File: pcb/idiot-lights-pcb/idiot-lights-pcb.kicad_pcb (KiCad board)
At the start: 2 copper layers, 100.3 x 66 mm, 35 parts, among them SW1 Toggle left indicator, SW2 Toggle right indicator, SW3 Toggle hazard warning, SW4 Break control, SW5 Reset

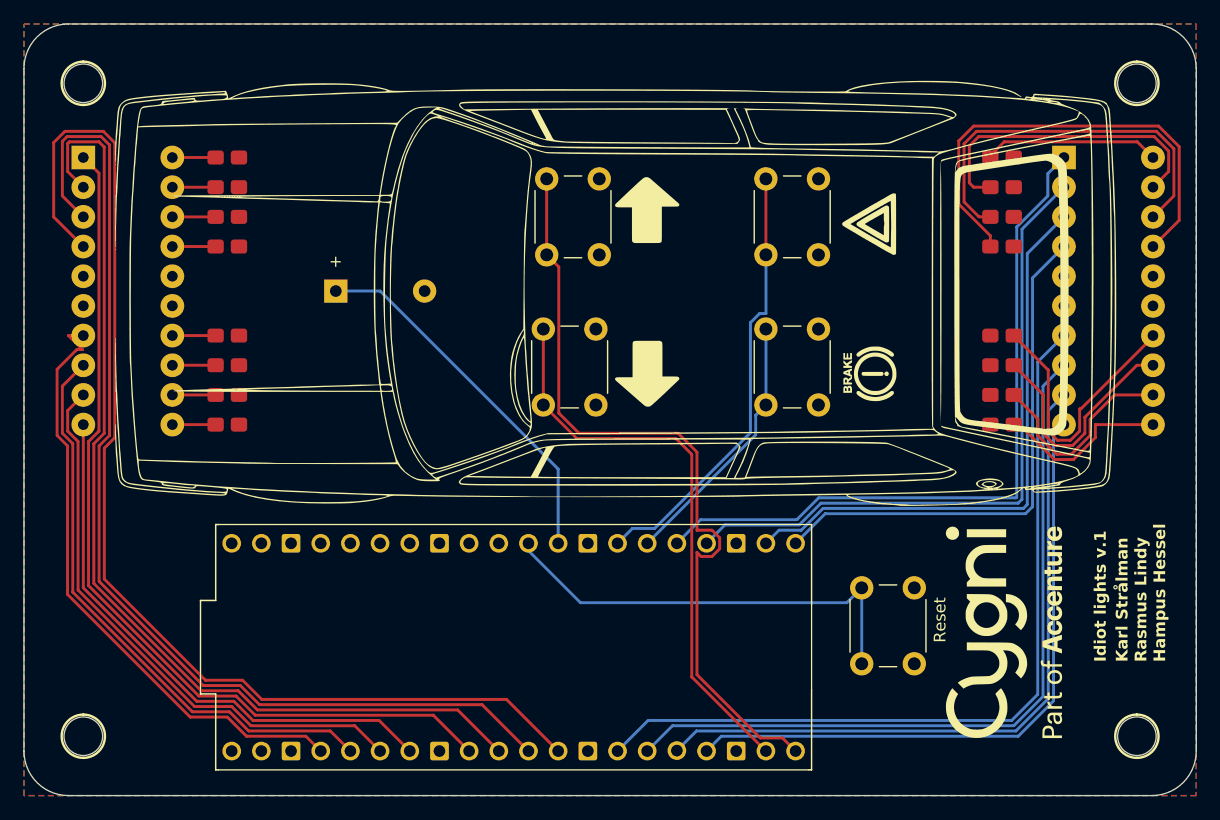
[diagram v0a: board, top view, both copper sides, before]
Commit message: Switch from THT to SMD for multiple components
Buzzer & LED lights arrays
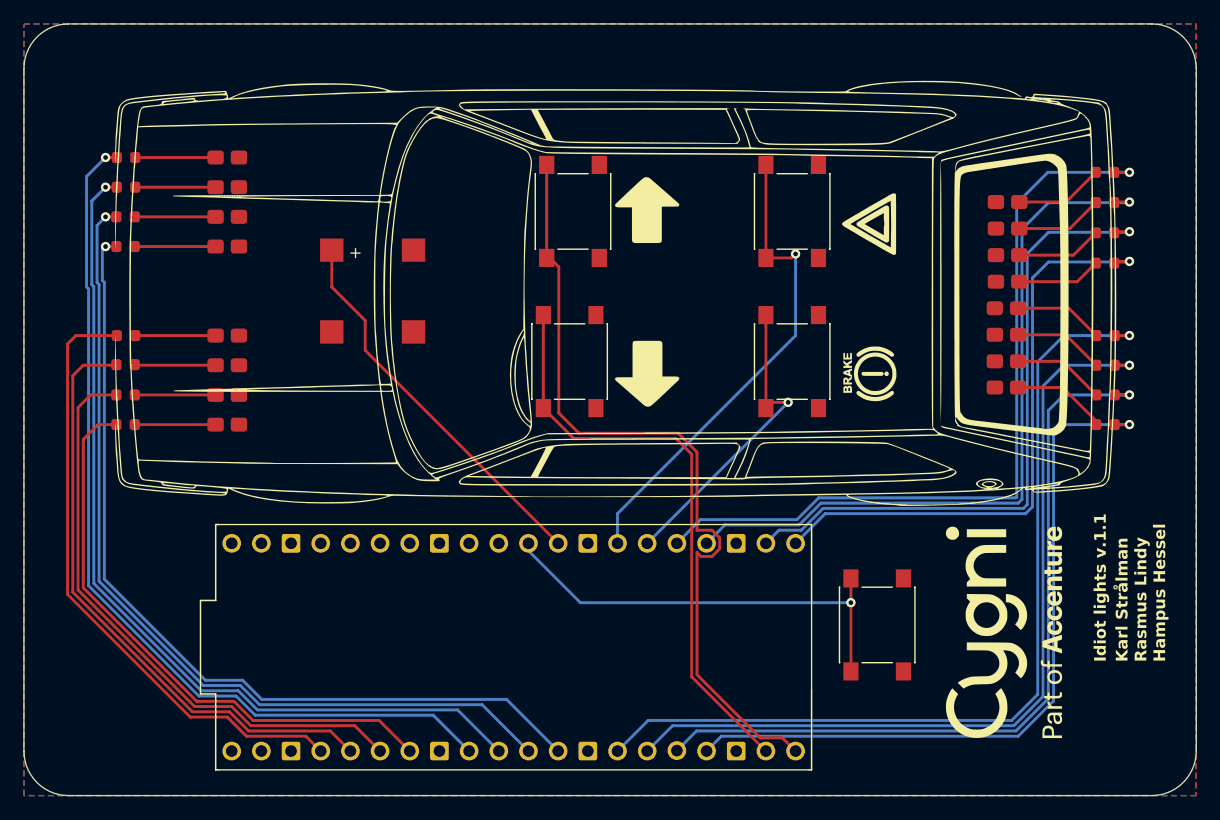
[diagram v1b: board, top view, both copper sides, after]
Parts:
- removed >NAME (x4): >VALUE, Hardware:STAND-OFF
- removed BAR1, BAR2: HDSP-4830_2, Display:HDSP-4830
- added D1: LED, LED_SMD_no_silk:LED_0603_1608Metric_no_silk, F.Cu at (143.3, 71.1)
- added D10: LED, LED_SMD_no_silk:LED_0603_1608Metric_no_silk, F.Cu at (227.2, 68.6)
- added D11: LED, LED_SMD_no_silk:LED_0603_1608Metric_no_silk, F.Cu at (227.2, 66.0)
- added D12: LED, LED_SMD_no_silk:LED_0603_1608Metric_no_silk, F.Cu at (227.2, 63.5)
- added D13: LED, LED_SMD_no_silk:LED_0603_1608Metric_no_silk, F.Cu at (227.1, 57.3)
- added D14: LED, LED_SMD_no_silk:LED_0603_1608Metric_no_silk, F.Cu at (227.1, 54.7)
- added D15: LED, LED_SMD_no_silk:LED_0603_1608Metric_no_silk, F.Cu at (227.1, 52.1)
- added D16: LED, LED_SMD_no_silk:LED_0603_1608Metric_no_silk, F.Cu at (227.1, 49.5)
- added D2: LED, LED_SMD_no_silk:LED_0603_1608Metric_no_silk, F.Cu at (143.3, 68.6)
- added D3: LED, LED_SMD_no_silk:LED_0603_1608Metric_no_silk, F.Cu at (143.3, 66.0)
- added D4: LED, LED_SMD_no_silk:LED_0603_1608Metric_no_silk, F.Cu at (143.4, 63.5)
- added D5: LED, LED_SMD_no_silk:LED_0603_1608Metric_no_silk, F.Cu at (143.3, 55.9)
- added D6: LED, LED_SMD_no_silk:LED_0603_1608Metric_no_silk, F.Cu at (143.3, 53.3)
- added D7: LED, LED_SMD_no_silk:LED_0603_1608Metric_no_silk, F.Cu at (143.4, 50.8)
- added D8: LED, LED_SMD_no_silk:LED_0603_1608Metric_no_silk, F.Cu at (143.4, 48.3)
- added D9: LED, LED_SMD_no_silk:LED_0603_1608Metric_no_silk, F.Cu at (227.2, 71.1)
- BZ1: footprint Buzzer_Beeper:Buzzer_12x9.5RM7.6 -> Buzzer_Beeper:PUIAudio_SMT_0825_S_4_R
- SW1, SW2, SW3, SW4, SW5: footprint Button_Switch_THT:SW_PUSH_6mm_H5mm -> Button_Switch_SMD:SW_SPST_PTS645
- moved SW1 4.34 mm to (181.3, 65.7)
- moved SW2 4.34 mm to (181.6, 52.9)
- moved SW3 4.34 mm to (200.4, 52.9)
- moved SW4 4.34 mm to (200.4, 65.7)
- moved R16 3.84 mm to (218.8, 52.1), turned to 180 degrees
- moved SW5 3.58 mm to (207.6, 88.3)
- moved R15 3.57 mm to (218.8, 54.3), turned to 180 degrees
- moved R14 3.31 mm to (218.8, 56.6), turned to 180 degrees
- moved R9 3.20 mm to (218.7, 67.9)
- moved BZ1 3.16 mm to (164.5, 59.7)
- moved R13 3.04 mm to (218.8, 58.9), turned to 180 degrees
- moved R10 2.90 mm to (218.7, 65.7)
- moved R11 2.64 mm to (218.7, 63.4)
- moved R12 2.37 mm to (218.7, 61.2)
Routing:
- net Net-(D13-K): track 39.8 -> 7.20 mm
- net Net-(D14-K): track 33.3 -> 7.33 mm
- net /FR3: track 98.6 -> 74.5 mm, vias 0 -> 1
- net Net-(D15-K): track 26.7 -> 7.47 mm
- net /FR2: track 92.2 -> 75.3 mm, vias 0 -> 1
- net Net-(D12-K): track 23.5 -> 7.65 mm
- net Net-(D11-K): track 20.4 -> 7.76 mm
- net /FR1: track 86.0 -> 76.0 mm, vias 0 -> 1
- net Net-(D10-K): track 17.8 -> 7.87 mm
- net Net-(D16-K): track 15.1 -> 7.60 mm
- net /RL3: track 55.5 -> 62.4 mm, vias 0 -> 1
- net /RL2: track 60.2 -> 67.1 mm, vias 0 -> 1
- net /RL0: track 69.6 -> 76.5 mm, vias 0 -> 1
- net /RL1: track 64.9 -> 71.8 mm, vias 0 -> 1
- net Net-(D9-K): track 15.0 -> 8.17 mm
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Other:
- board text added: "Idiot lights v.1.1"
- board text removed: "Idiot lights v.1"

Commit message: Add pico SMD solder mounts
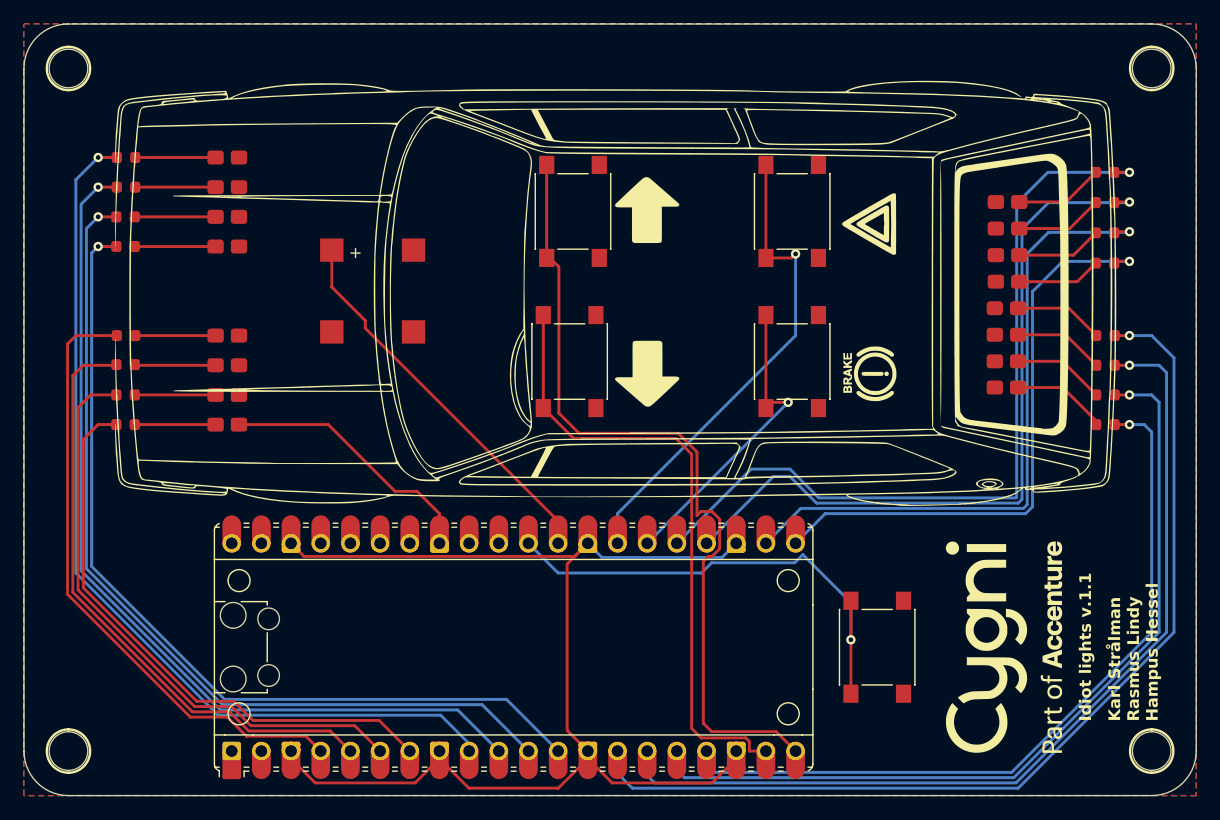
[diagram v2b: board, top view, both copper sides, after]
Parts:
- removed A1: SC0915, Raspberry_Pi_Pico_Kicad_Files:MODULE_SC0915
- added >NAME: >VALUE, Hardware:STAND-OFF, F.Cu at (138.4, 99.1)
- added >NAME: >VALUE, Hardware:STAND-OFF, F.Cu at (231.1, 99.1)
- added >NAME: >VALUE, Hardware:STAND-OFF, F.Cu at (231.1, 40.6)
- added >NAME: >VALUE, Hardware:STAND-OFF, F.Cu at (138.4, 40.6)
- added U1: RaspberryPi_Pico, Module_RaspberryPi_Pico:RaspberryPi_Pico_Common, F.Cu at (176.5, 90.2)
- moved SW5 1.91 mm to (207.6, 90.2)
- moved G*** 1.27 mm to (218.4, 90.2)
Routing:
- net Net-(U1-GND-Pad13): track 0.00 -> 105.5 mm
- net GND: track 0.00 -> 22.9 mm
- net /RL0: track 76.5 -> 84.9 mm
- net /RL1: track 71.8 -> 79.1 mm
- net /RL2: track 67.1 -> 72.1 mm
- net /RUN: track 37.8 -> 42.1 mm
- net /L_INDCR_BTN: track 50.1 -> 53.1 mm
- net /RL3: track 62.4 -> 65.1 mm
- net /RR0: track 67.9 -> 70.0 mm
- net /RR1: track 63.2 -> 65.1 mm
- net /FR0: track 76.8 -> 78.3 mm
- net /FR3: track 74.5 -> 75.6 mm
- net /FR1: track 76.0 -> 77.2 mm
- net /FR2: track 75.3 -> 76.4 mm
- net /R_INDCR_BTN: track 69.0 -> 70.1 mm
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
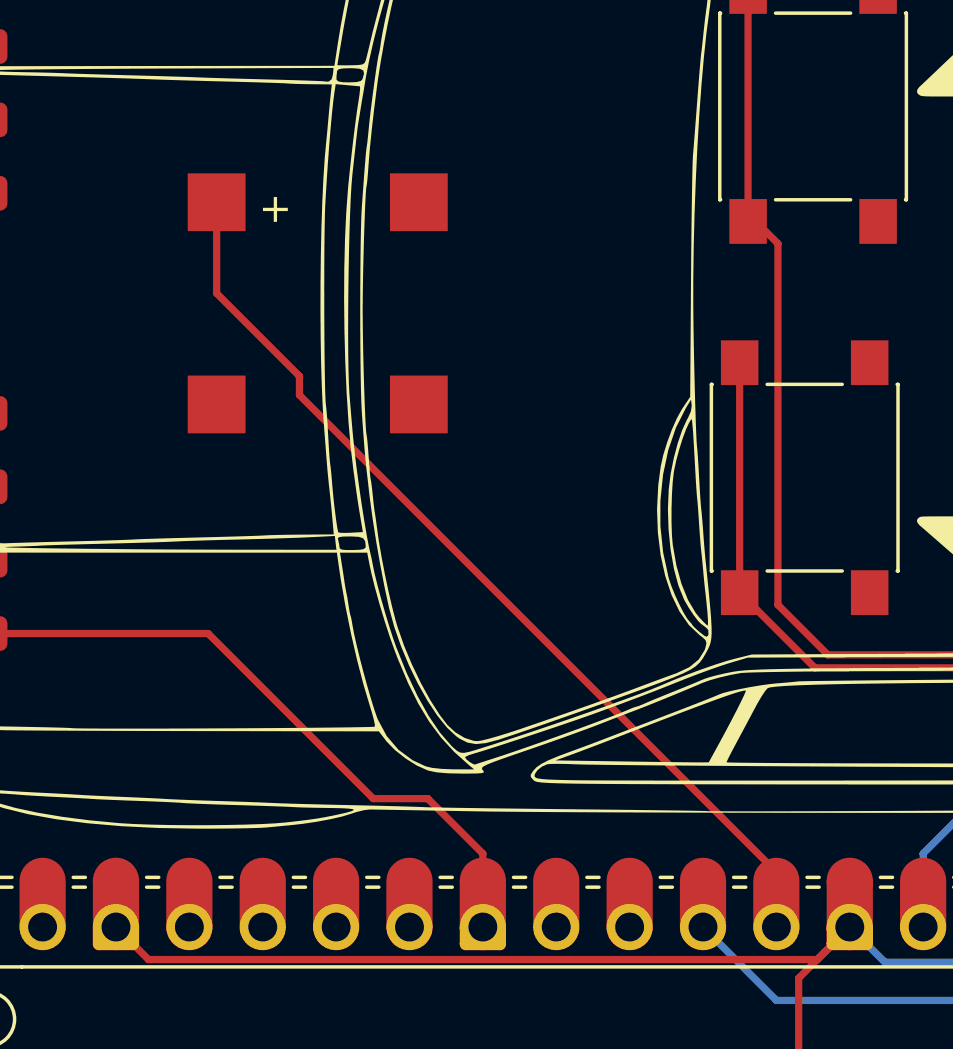
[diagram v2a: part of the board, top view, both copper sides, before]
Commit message: Replace buzzer with CPT
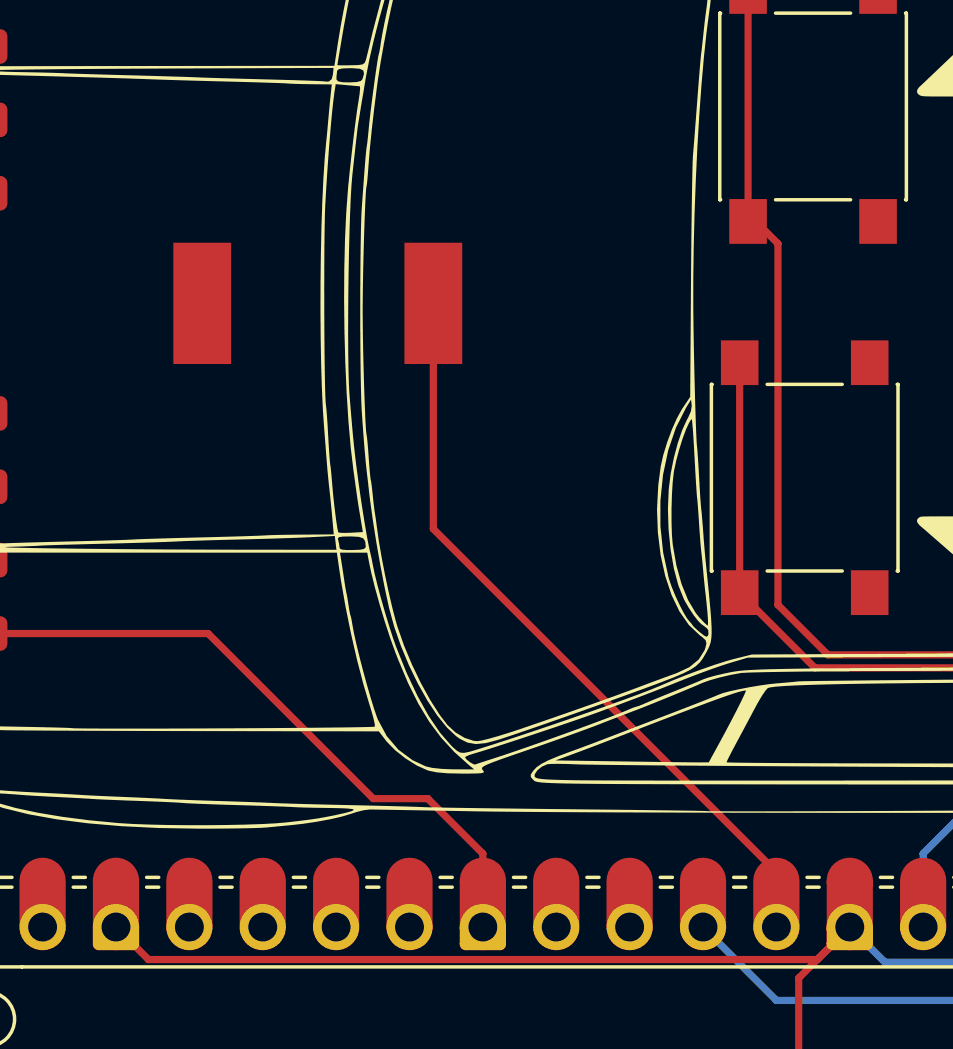
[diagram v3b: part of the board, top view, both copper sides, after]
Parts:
- BZ1: footprint Buzzer_Beeper:PUIAudio_SMT_0825_S_4_R -> Buzzer_Beeper:Buzzer_CUI_CPT-9019S-SMT
- turned BZ1 to 180 degrees
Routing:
- net /BUZZER: track 33.1 -> 26.5 mm
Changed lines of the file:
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@@
     )
   )
-  (footprint "Buzzer_Beeper:PUIAudio_SMT_0825_S_4_R" (layer "F.Cu")
-    (at 164.465 59.69)
-    (descr "SMD 8540, http://www.puiaudio.com/product-detail.aspx?partnumber=SMT-0825-S-4-R")
-    (tags "SMD 8540")
+  (footprint "Buzzer_Beeper:Buzzer_CUI_CPT-9019S-SMT" (layer "F.Cu")
+    (at 164.465 59.69 180)
+    (descr "https://www.cui.com/product/resource/cpt-9019s-smt.pdf")
+    (tags "buzzer piezo")
     (property "Sheetfile" "idiot-lights-pcb.kicad_sch")
     (property "Sheetname" "")
@@
     (property "ki_keywords" "quartz resonator ceramic")
     (attr smd)
-    (fp_text reference "BZ1" (at 0.2 -5.9) (layer "F.SilkS") hide
+    (fp_text reference "BZ1" (at 0 -5.5) (layer "F.SilkS") hide
         (effects (font (size 1 1) (thickness 0.15)))
     )
-    (fp_text value "Buzzer" (at 0.1 6) (layer "F.Fab") hide
-        (effects (font (size 1 1) (thickness 0.15)))
-    )
-    (fp_text user "+" (at -1.5 -3.25 270) (layer "F.SilkS")
-        (effects (font (size 1 1) (thickness 0.15)))
-    )
-    (fp_text user "+" (at -2.75 -2.75 270) (layer "F.Fab")
+    (fp_text value "Buzzer" (at 0 5.5) (layer "F.Fab") hide
         (effects (font (size 1 1) (thickness 0.15)))
     )
+    (fp_line (start -5.25 -2.35) (end -4.75 -2.35)
+      (stroke (width 0.05) (type solid)) (layer "F.CrtYd"))
+    (fp_line (start -5.25 2.35) (end -5.25 -2.35)
+      (stroke (width 0.05) (type solid)) (layer "F.CrtYd"))
     (fp_line (start -4.75 -4.75) (end 4.75 -4.75)
       (stroke (width 0.05) (type solid)) (layer "F.CrtYd"))
-    (fp_line (start -4.75 4.75) (end -4.75 -4.75)
+    (fp_line (start -4.75 -2.35) (end -4.75 -4.75)
+      (stroke (width 0.05) (type solid)) (layer "F.CrtYd"))
+    (fp_line (start -4.75 2.35) (end -5.25 2.35)
+      (stroke (width 0.05) (type solid)) (layer "F.CrtYd"))
+    (fp_line (start -4.75 4.75) (end -4.75 2.35)
       (stroke (width 0.05) (type solid)) (layer "F.CrtYd"))
-    (fp_line (start 4.75 -4.75) (end 4.75 4.75)
+    (fp_line (start 4.75 -4.75) (end 4.75 -2.35)
+      (stroke (width 0.05) (type solid)) (layer "F.CrtYd"))
+    (fp_line (start 4.75 -2.35) (end 5.25 -2.35)
+      (stroke (width 0.05) (type solid)) (layer "F.CrtYd"))
+    (fp_line (start 4.75 2.35) (end 4.75 4.75)
       (stroke (width 0.05) (type solid)) (layer "F.CrtYd"))
     (fp_line (start 4.75 4.75) (end -4.75 4.75)
       (stroke (width 0.05) (type solid)) (layer "F.CrtYd"))
-    (fp_line (start -4.25 -2.75) (end -2.75 -4.25)
-      (stroke (width 0.1) (type solid)) (layer "F.Fab"))
-    (fp_line (start -4.25 2.75) (end -4.25 -2.75)
-      (stroke (width 0.1) (type solid)) (layer "F.Fab"))
-    (fp_line (start -2.75 -4.25) (end 2.75 -4.25)
-      (stroke (width 0.1) (type solid)) (layer "F.Fab"))
-    (fp_line (start -2.75 4.25) (end -4.25 2.75)
+    (fp_line (start 5.25 -2.35) (end 5.25 2.35)
+      (stroke (width 0.05) (type solid)) (layer "F.CrtYd"))
+    (fp_line (start 5.25 2.35) (end 4.75 2.35)
+      (stroke (width 0.05) (type solid)) (layer "F.CrtYd"))
+    (fp_line (start -4.5 -3.5) (end -4.5 4.5)
       (stroke (width 0.1) (type solid)) (layer "F.Fab"))
-    (fp_line (start 2.75 -4.25) (end 4.25 -2.75)
+    (fp_line (start -4.5 4.5) (end 4.5 4.5)
       (stroke (width 0.1) (type solid)) (layer "F.Fab"))
-    (fp_line (start 2.75 4.25) (end -2.75 4.25)
+    (fp_line (start -3.5 -4.5) (end -4.5 -3.5)
       (stroke (width 0.1) (type solid)) (layer "F.Fab"))
-    (fp_line (start 4.25 -2.75) (end 4.25 2.75)
+    (fp_line (start 4.5 -4.5) (end -3.5 -4.5)
       (stroke (width 0.1) (type solid)) (layer "F.Fab"))
-    (fp_line (start 4.25 2.75) (end 2.75 4.25)
+    (fp_line (start 4.5 4.5) (end 4.5 -4.5)
       (stroke (width 0.1) (type solid)) (layer "F.Fab"))
-    (pad "1" smd rect (at -3.5 -3.5 270) (size 2 2) (layers "F.Cu" "F.Paste" "F.Mask")
+    (pad "1" smd rect (at -4 0 180) (size 2 4.2) (layers "F.Cu" "F.Paste" "F.Mask")
       (net 4 "/BUZZER") (pinfunction "-") (pintype "passive"))
-    (pad "2" smd rect (at -3.5 3.5 270) (size 2 2) (layers "F.Cu" "F.Paste" "F.Mask")
+    (pad "2" smd rect (at 4 0 180) (size 2 4.2) (layers "F.Cu" "F.Paste" "F.Mask")
       (net 1 "GND") (pinfunction "+") (pintype "passive"))
-    (pad "3" smd rect (at 3.5 3.5 270) (size 2 2) (layers "F.Cu" "F.Paste" "F.Mask"))
-    (pad "4" smd rect (at 3.5 -3.5 270) (size 2 2) (layers "F.Cu" "F.Paste" "F.Mask"))
-    (model "${KICAD6_3DMODEL_DIR}/Buzzer_Beeper.3dshapes/PUIAudio_SMT_0825_S_4_R.wrl"
+    (model "${KICAD6_3DMODEL_DIR}/Buzzer_Beeper.3dshapes/Buzzer_CUI_CPT-9019S-SMT.wrl"
       (offset (xyz 0 0 0))
       (scale (xyz 1 1 1))
@@
   (via (at 200.025 69.215) (size 0.8) (drill 0.4) (layers "F.Cu" "B.Cu") (net 3))
   (segment (start 187.96 81.28) (end 200.025 69.215) (width 0.25) (layer "B.Cu") (net 3))
-  (segment (start 163.83 62.21) (end 160.965 59.345) (width 0.25) (layer "F.Cu") (net 4))
-  (segment (start 163.83 62.865) (end 163.83 62.21) (width 0.25) (layer "F.Cu") (net 4))
-  (segment (start 180.34 79.375) (end 163.83 62.865) (width 0.25) (layer "F.Cu") (net 4))
+  (segment (start 168.465 67.5) (end 168.465 59.69) (width 0.25) (layer "F.Cu") (net 4))
+  (segment (start 180.34 79.375) (end 168.465 67.5) (width 0.25) (layer "F.Cu") (net 4))
   (segment (start 180.34 81.28) (end 180.34 79.375) (width 0.25) (layer "F.Cu") (net 4))
-  (segment (start 160.965 59.345) (end 160.965 56.19) (width 0.25) (layer "F.Cu") (net 4))
   (segment (start 205.395 89.535) (end 205.395 94.15) (width 0.25) (layer "F.Cu") (net 5))
   (segment (start 205.395 89.535) (end 205.395 86.19) (width 0.25) (layer "F.Cu") (net 5))
